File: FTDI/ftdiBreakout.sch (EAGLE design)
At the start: 8 parts, among them X1 USBSMD

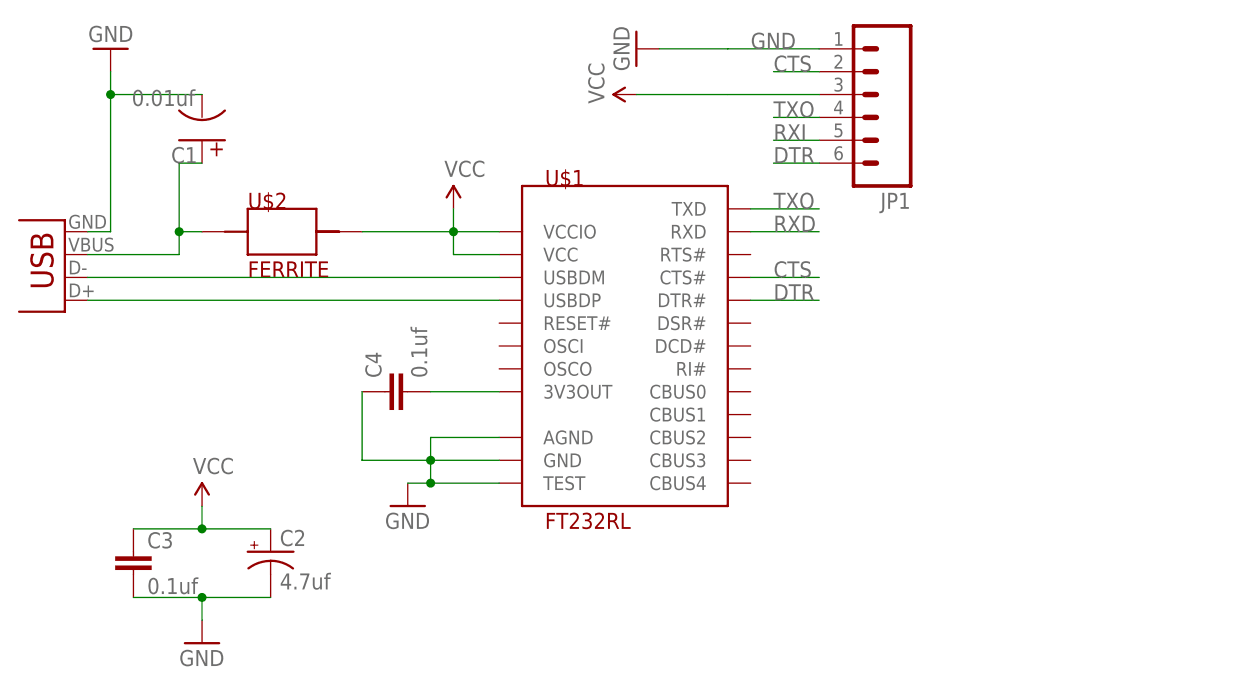
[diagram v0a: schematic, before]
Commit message: added barrel connector and touched up top silk
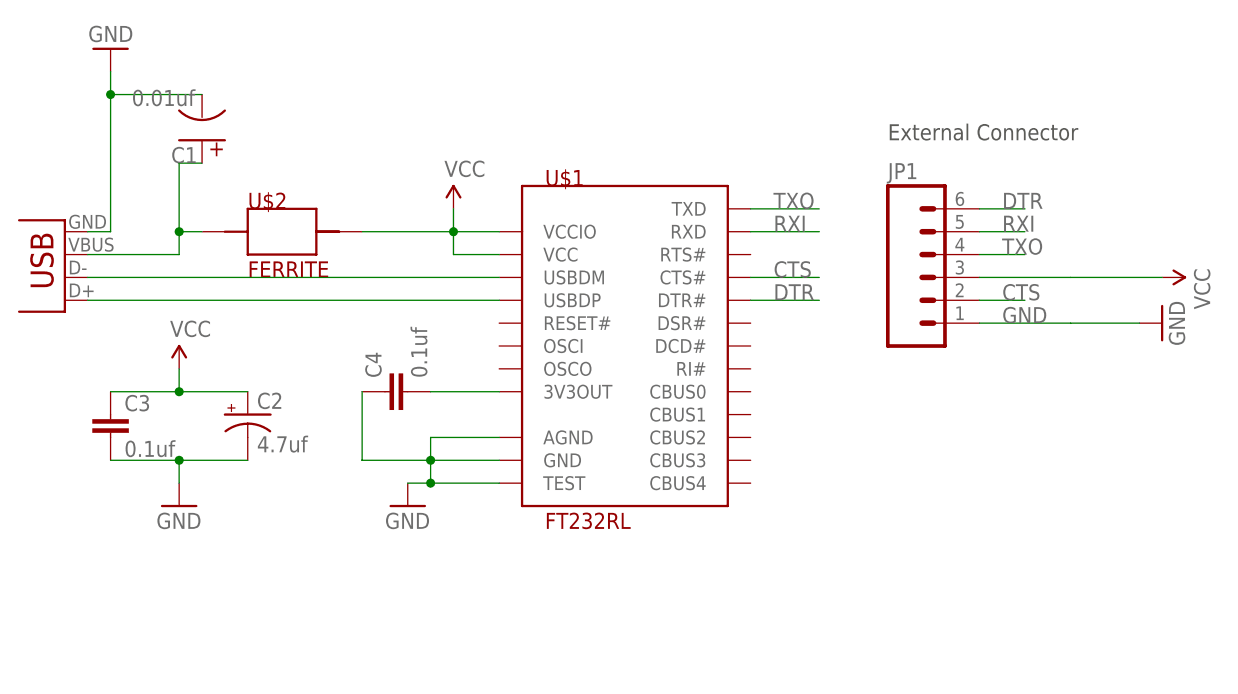
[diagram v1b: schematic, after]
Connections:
- removed net RXD: U$1.RXD
- net RXI: now also U$1.RXD
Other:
- note added: "External Connector"
- moved on the sheet: C2, C3, JP1
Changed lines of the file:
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@@
 <layer number="203" name="203bmp" color="4" fill="10" visible="no" active="yes"/>
 <layer number="204" name="204bmp" color="5" fill="10" visible="no" active="yes"/>
-<layer number="205" name="205bmp" color="6" fill="10" visible="no" active="yes"/>
+<layer number="205" name="205bmp" color="6" fill="10" visible="yes" active="yes"/>
 <layer number="206" name="206bmp" color="7" fill="10" visible="no" active="yes"/>
 <layer number="207" name="207bmp" color="8" fill="10" visible="no" active="yes"/>
@@
 <sheet>
 <plain>
+<text x="104.14" y="96.52" size="1.778" layer="92">External Connector</text>
 </plain>
 <instances>
@@
 <instance part="GND2" gate="1" x="17.78" y="106.68" rot="R180"/>
 <instance part="P+1" gate="1" x="55.88" y="88.9"/>
-<instance part="GND3" gate="1" x="27.94" y="40.64"/>
-<instance part="P+3" gate="1" x="27.94" y="55.88"/>
+<instance part="GND3" gate="1" x="25.4" y="55.88"/>
+<instance part="P+3" gate="1" x="25.4" y="71.12"/>
 <instance part="C1" gate="C$1" x="27.94" y="99.06" rot="R180"/>
-<instance part="C2" gate="G$1" x="35.56" y="50.8"/>
-<instance part="C3" gate="G$1" x="20.32" y="48.26"/>
+<instance part="C2" gate="G$1" x="33.02" y="66.04"/>
+<instance part="C3" gate="G$1" x="17.78" y="63.5"/>
 <instance part="C4" gate="G$1" x="50.8" y="68.58" rot="R90"/>
-<instance part="JP1" gate="G$1" x="101.6" y="101.6" rot="R180"/>
-<instance part="P+2" gate="1" x="76.2" y="101.6" rot="R90"/>
-<instance part="GND4" gate="1" x="76.2" y="106.68" rot="R270"/>
+<instance part="JP1" gate="G$1" x="109.22" y="81.28"/>
+<instance part="P+2" gate="1" x="134.62" y="81.28" rot="R270"/>
+<instance part="GND4" gate="1" x="134.62" y="76.2" rot="R90"/>
 </instances>
 <busses>
@@
 <pinref part="C2" gate="G$1" pin="-"/>
 <pinref part="C3" gate="G$1" pin="2"/>
-<wire x1="35.56" y1="45.72" x2="27.94" y2="45.72" width="0.1524" layer="91"/>
-<junction x="27.94" y="45.72"/>
-<wire x1="27.94" y1="45.72" x2="20.32" y2="45.72" width="0.1524" layer="91"/>
+<wire x1="33.02" y1="60.96" x2="25.4" y2="60.96" width="0.1524" layer="91"/>
+<junction x="25.4" y="60.96"/>
+<wire x1="25.4" y1="60.96" x2="17.78" y2="60.96" width="0.1524" layer="91"/>
 <pinref part="GND3" gate="1" pin="GND"/>
-<wire x1="27.94" y1="45.72" x2="27.94" y2="43.18" width="0.1524" layer="91"/>
+<wire x1="25.4" y1="60.96" x2="25.4" y2="58.42" width="0.1524" layer="91"/>
 </segment>
 <segment>
 <pinref part="JP1" gate="G$1" pin="1"/>
-<wire x1="96.52" y1="106.68" x2="86.36" y2="106.68" width="0.1524" layer="91"/>
-<label x="88.9" y="106.68" size="1.778" layer="95"/>
+<wire x1="114.3" y1="76.2" x2="124.46" y2="76.2" width="0.1524" layer="91"/>
+<label x="116.84" y="76.2" size="1.778" layer="95"/>
 <pinref part="GND4" gate="1" pin="GND"/>
-<wire x1="86.36" y1="106.68" x2="78.74" y2="106.68" width="0.1524" layer="91"/>
+<wire x1="124.46" y1="76.2" x2="132.08" y2="76.2" width="0.1524" layer="91"/>
 </segment>
 </net>
@@
 <pinref part="C2" gate="G$1" pin="+"/>
 <pinref part="C3" gate="G$1" pin="1"/>
-<wire x1="35.56" y1="53.34" x2="27.94" y2="53.34" width="0.1524" layer="91"/>
-<junction x="27.94" y="53.34"/>
-<wire x1="27.94" y1="53.34" x2="20.32" y2="53.34" width="0.1524" layer="91"/>
+<wire x1="33.02" y1="68.58" x2="25.4" y2="68.58" width="0.1524" layer="91"/>
+<junction x="25.4" y="68.58"/>
+<wire x1="25.4" y1="68.58" x2="17.78" y2="68.58" width="0.1524" layer="91"/>
 <pinref part="P+3" gate="1" pin="VCC"/>
-<wire x1="27.94" y1="53.34" x2="27.94" y2="55.88" width="0.1524" layer="91"/>
+<wire x1="25.4" y1="68.58" x2="25.4" y2="71.12" width="0.1524" layer="91"/>
 </segment>
 <segment>
 <pinref part="JP1" gate="G$1" pin="3"/>
-<wire x1="96.52" y1="101.6" x2="86.36" y2="101.6" width="0.1524" layer="91"/>
+<wire x1="114.3" y1="81.28" x2="124.46" y2="81.28" width="0.1524" layer="91"/>
 <pinref part="P+2" gate="1" pin="VCC"/>
-<wire x1="86.36" y1="101.6" x2="76.2" y2="101.6" width="0.1524" layer="91"/>
+<wire x1="124.46" y1="81.28" x2="134.62" y2="81.28" width="0.1524" layer="91"/>
 </segment>
 </net>
@@
 <segment>
 <pinref part="JP1" gate="G$1" pin="4"/>
-<wire x1="96.52" y1="99.06" x2="91.44" y2="99.06" width="0.1524" layer="91"/>
-<label x="91.44" y="99.06" size="1.778" layer="95"/>
+<wire x1="114.3" y1="83.82" x2="119.38" y2="83.82" width="0.1524" layer="91"/>
+<label x="116.84" y="83.82" size="1.778" layer="95"/>
 </segment>
 <segment>
@@
 </segment>
 </net>
-<net name="RXD" class="0">
+<net name="CTS" class="0">
+<segment>
+<pinref part="JP1" gate="G$1" pin="2"/>
+<wire x1="114.3" y1="78.74" x2="119.38" y2="78.74" width="0.1524" layer="91"/>
+<label x="116.84" y="78.74" size="1.778" layer="95"/>
+</segment>
+<segment>
+<pinref part="U$1" gate="G$1" pin="CTS#"/>
+<wire x1="96.52" y1="81.28" x2="88.9" y2="81.28" width="0.1524" layer="91"/>
+<label x="91.44" y="81.28" size="1.778" layer="95"/>
+</segment>
+</net>
+<net name="DTR" class="0">
+<segment>
+<pinref part="JP1" gate="G$1" pin="6"/>
+<wire x1="114.3" y1="88.9" x2="119.38" y2="88.9" width="0.1524" layer="91"/>
+<label x="116.84" y="88.9" size="1.778" layer="95"/>
+</segment>
+<segment>
+<pinref part="U$1" gate="G$1" pin="DTR#"/>
+<wire x1="88.9" y1="78.74" x2="96.52" y2="78.74" width="0.1524" layer="91"/>
+<label x="91.44" y="78.74" size="1.778" layer="95"/>
+</segment>
+</net>
+<net name="RXI" class="0">
+<segment>
+<pinref part="JP1" gate="G$1" pin="5"/>
+<wire x1="114.3" y1="86.36" x2="119.38" y2="86.36" width="0.1524" layer="91"/>
+<label x="116.84" y="86.36" size="1.778" layer="95"/>
+</segment>
 <segment>
 <pinref part="U$1" gate="G$1" pin="RXD"/>
@@
 </segment>
 </net>
-<net name="CTS" class="0">
-<segment>
-<pinref part="JP1" gate="G$1" pin="2"/>
-<wire x1="96.52" y1="104.14" x2="91.44" y2="104.14" width="0.1524" layer="91"/>
-<label x="91.44" y="104.14" size="1.778" layer="95"/>
-</segment>
-<segment>
-<pinref part="U$1" gate="G$1" pin="CTS#"/>
-<wire x1="96.52" y1="81.28" x2="88.9" y2="81.28" width="0.1524" layer="91"/>
-<label x="91.44" y="81.28" size="1.778" layer="95"/>
-</segment>
-</net>
-<net name="DTR" class="0">
-<segment>
-<pinref part="JP1" gate="G$1" pin="6"/>
-<wire x1="96.52" y1="93.98" x2="91.44" y2="93.98" width="0.1524" layer="91"/>
-<label x="91.44" y="93.98" size="1.778" layer="95"/>
-</segment>
-<segment>
-<pinref part="U$1" gate="G$1" pin="DTR#"/>
-<wire x1="88.9" y1="78.74" x2="96.52" y2="78.74" width="0.1524" layer="91"/>
-<label x="91.44" y="78.74" size="1.778" layer="95"/>
-</segment>
-</net>
-<net name="RXI" class="0">
-<segment>
-<pinref part="JP1" gate="G$1" pin="5"/>
-<wire x1="96.52" y1="96.52" x2="91.44" y2="96.52" width="0.1524" layer="91"/>
-<label x="91.44" y="96.52" size="1.778" layer="95"/>
-</segment>
-</net>

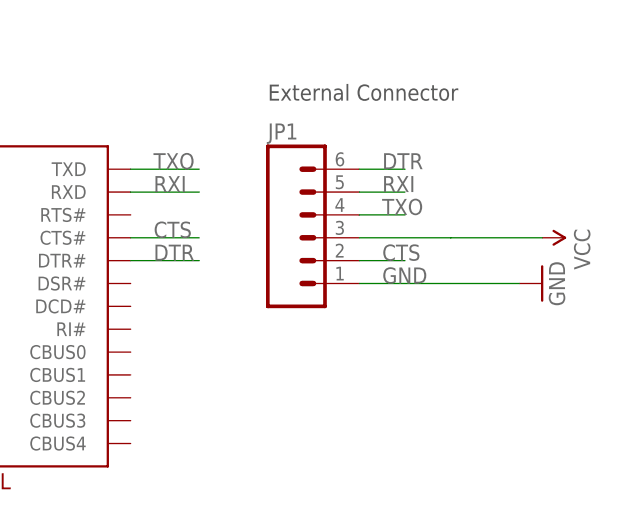
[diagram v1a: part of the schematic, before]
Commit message: Tested versions of breakout boards
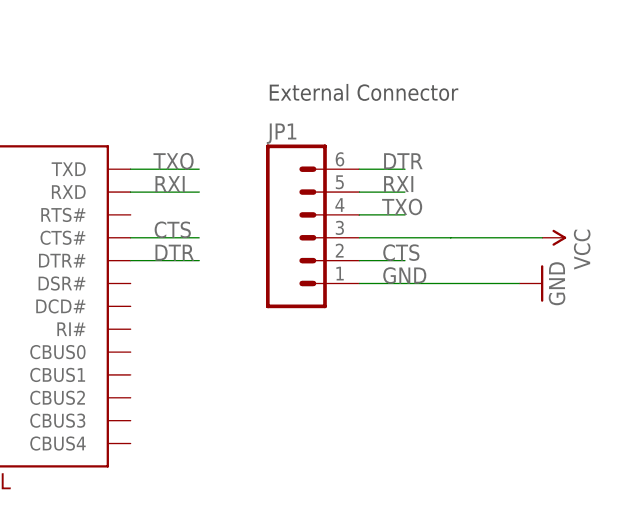
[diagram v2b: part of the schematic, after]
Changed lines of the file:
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@@
 <segment>
 <pinref part="JP1" gate="G$1" pin="1"/>
-<wire x1="114.3" y1="76.2" x2="124.46" y2="76.2" width="0.1524" layer="91"/>
+<wire x1="114.3" y1="76.2" x2="116.84" y2="76.2" width="0.1524" layer="91"/>
 <label x="116.84" y="76.2" size="1.778" layer="95"/>
 <pinref part="GND4" gate="1" pin="GND"/>
+<wire x1="116.84" y1="76.2" x2="124.46" y2="76.2" width="0.1524" layer="91"/>
 <wire x1="124.46" y1="76.2" x2="132.08" y2="76.2" width="0.1524" layer="91"/>
 </segment>
